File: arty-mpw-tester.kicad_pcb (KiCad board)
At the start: 4 copper layers, 53.3 x 61.5 mm, 174 parts, among them J1 USB4105-GF-A, J10 61300211121, J11 61300211121, J12 61300211121, J14 61300311121, J15 61300311121, J18 61300411121, J19 61300711121, J20 61300411121, J3 arty_chipKIT_connector, J4 61300211121, J5 61300311121, J6 61300211121, J7 61300211121, J8 61300211121, J9 61300211121, Q1 DTC014TEBTL, SW1 JS202011JCQN, SW3 JS202011JCQN, U1 PAC1954T-E/4MX, U10 TPD4E02B04DQA, U11 TAR5S33UTE85LF, U2 FT4232H-56Q, U3 PAC1954T-E/4MX, U4 MAX811REUS+T, U5 NTS0102DP, U6 MCP4661-103E/ML, U7 Caravel_breakout_PCB_flexypin, U8 W25Q32FVSS, U9 MIC2211-AAYML-TR, Y1 ABM8G-12.000MHZ-18-D2Y-T, Y2 ECS-2520MVLC-100-BN-TR

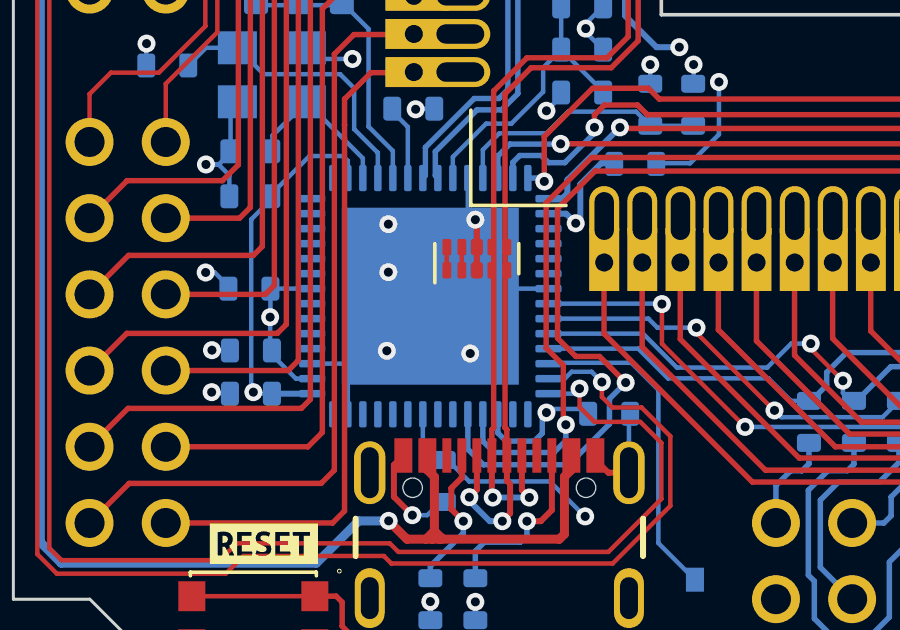
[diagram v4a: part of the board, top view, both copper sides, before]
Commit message: Adjusted USB TVS position
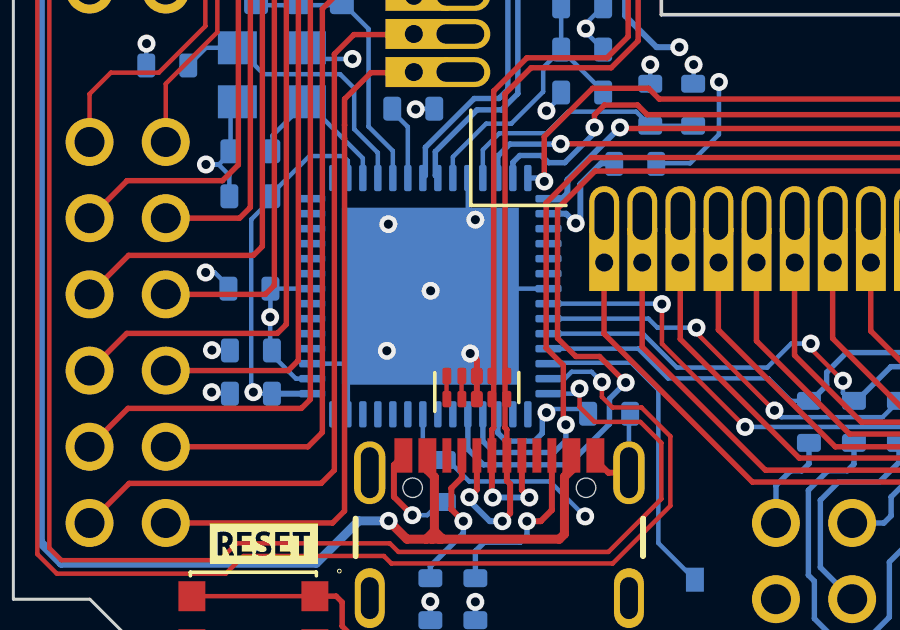
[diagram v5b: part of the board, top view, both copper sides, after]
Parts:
- moved U10 4.29 mm to (138.4, 117.9)
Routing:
- net EP: track 94.6 -> 92.9 mm
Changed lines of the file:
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@@
   )
   (footprint "arty-mpw-tester-footprints:USON-10_2.5x1.0mm_P0.5mm" (layer "F.Cu")
-    (at 138.45 113.65 90)
+    (at 138.45 117.945 90)
     (descr "USON-10 2.5x1.0mm_ Pitch 0.5mm http://www.ti.com/lit/ds/symlink/tpd4e02b04.pdf")
     (tags "USON-10 2.5x1.0mm Pitch 0.5mm")
@@
   (segment (start 131.63 83.49) (end 131.43 83.29) (width 0.2) (layer "B.Cu") (net 15))
   (segment (start 158.13 75.44) (end 158.25 75.56) (width 0.2) (layer "B.Cu") (net 15))
+  (segment (start 138.44 118.33) (end 138.45 118.32) (width 0.2) (layer "F.Cu") (net 17))
   (segment (start 135.684999 120.525001) (end 135.684999 121.584999) (width 0.2) (layer "F.Cu") (net 17))
-  (segment (start 138.45 114.035) (end 138.45 112.4) (width 0.2) (layer "F.Cu") (net 17))
   (segment (start 128.95 126.5) (end 129.9 126.5) (width 0.2) (layer "F.Cu") (net 17))
   (segment (start 135.684999 121.584999) (end 136.3 122.2) (width 0.2) (layer "F.Cu") (net 17))
-  (segment (start 138.45 114.035) (end 138.45 113.265) (width 0.15) (layer "F.Cu") (net 17))
+  (segment (start 138.45 117.57) (end 138.44 117.56) (width 0.15) (layer "F.Cu") (net 17))
   (segment (start 143.52 120.785) (end 142.835 120.785) (width 0.2) (layer "F.Cu") (net 17))
   (segment (start 135.7 84.77) (end 135.7 83.2) (width 0.2) (layer "F.Cu") (net 17))
+  (segment (start 138.45 118.32) (end 138.45 117.03) (width 0.2) (layer "F.Cu") (net 17))
   (segment (start 133.05 126.5) (end 132.1 126.5) (width 0.2) (layer "F.Cu") (net 17))
+  (segment (start 138.45 117.03) (end 138.23 116.81) (width 0.2) (layer "F.Cu") (net 17))
   (segment (start 142.835 120.785) (end 142.4 120.35) (width 0.2) (layer "F.Cu") (net 17))
-  (segment (start 138.45 113.265) (end 138.45 112.4) (width 0.15) (layer "F.Cu") (net 17))
   (segment (start 136 120.21) (end 135.684999 120.525001) (width 0.2) (layer "F.Cu") (net 17))
-  (segment (start 138.45 112.4) (end 138.4 112.35) (width 0.2) (layer "F.Cu") (net 17))
   (via (at 132.93 74.29) (size 0.6) (drill 0.3) (layers "F.Cu" "B.Cu") (net 17))
   (via (at 145.35 90.368) (size 0.6) (drill 0.3) (layers "F.Cu" "B.Cu") (net 17))
@@
   (via (at 175.7 74.4) (size 0.6) (drill 0.3) (layers "F.Cu" "B.Cu") (net 17))
   (via (at 129.42 110.5095) (size 0.6) (drill 0.3) (layers "F.Cu" "B.Cu") (net 17))
-  (via (at 135.5 114.1) (size 0.6) (drill 0.3) (layers "F.Cu" "B.Cu") (net 17))
+  (via (at 136.91 114.72) (size 0.6) (drill 0.3) (layers "F.Cu" "B.Cu") (net 17))
   (via (at 129.62 116.7) (size 0.6) (drill 0.3) (layers "F.Cu" "B.Cu") (net 17))
   (via (at 156.55 90.368) (size 0.6) (drill 0.3) (layers "F.Cu" "B.Cu") (net 17))
@@
   (segment (start 169.75 105.9) (end 172.58 105.9) (width 0.182) (layer "F.Cu") (net 110))
   (segment (start 165.55 107.43) (end 164 107.43) (width 0.182) (layer "F.Cu") (net 110))
-  (segment (start 137.45 114.035) (end 137.45 113.265) (width 0.15) (layer "F.Cu") (net 113))
-  (segment (start 137.95 114.035) (end 137.95 113.265) (width 0.15) (layer "F.Cu") (net 114))
+  (segment (start 137.44 118.33) (end 137.44 117.56) (width 0.15) (layer "F.Cu") (net 113))
+  (segment (start 137.94 118.33) (end 137.94 117.56) (width 0.15) (layer "F.Cu") (net 114))
   (segment (start 158.445 116.295) (end 157.93 115.78) (width 0.182) (layer "F.Cu") (net 115))
   (segment (start 167.1 110.7) (end 167.1 115.9) (width 0.182) (layer "F.Cu") (net 115))
